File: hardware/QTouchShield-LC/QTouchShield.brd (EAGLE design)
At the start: 101.6 x 81.3 mm, 56 parts, among them IC1 AT32UC3C0512CJEDEC-MS-026, J1 SNS00...07, J10 CAPS08...15, J11 CAPS24...31, J12 CAPS16...23, J13 SPI-MEGA, J14 SPI-UNO, J15 COMMS Select, J16 DETECT00...15, J17 DETECT16...31, J18 JTAG, J19 TOUCH DATA, J2 SNS08...15, J3 SNS16...23, J4 SNS24...31, J5 RES00...07, J6 RES08...15, J7 RES16...23, J8 RES24...31, J9 CAPS00...07, Q1 BSS138, Q2 BSS138, Q3 BSS138, Q4 BSS138, Q5 BSS138, Q6 BSS138, U1 ARDUINO-2560-MEGA-R3-SMD, X1 Firmware Upgrade Port

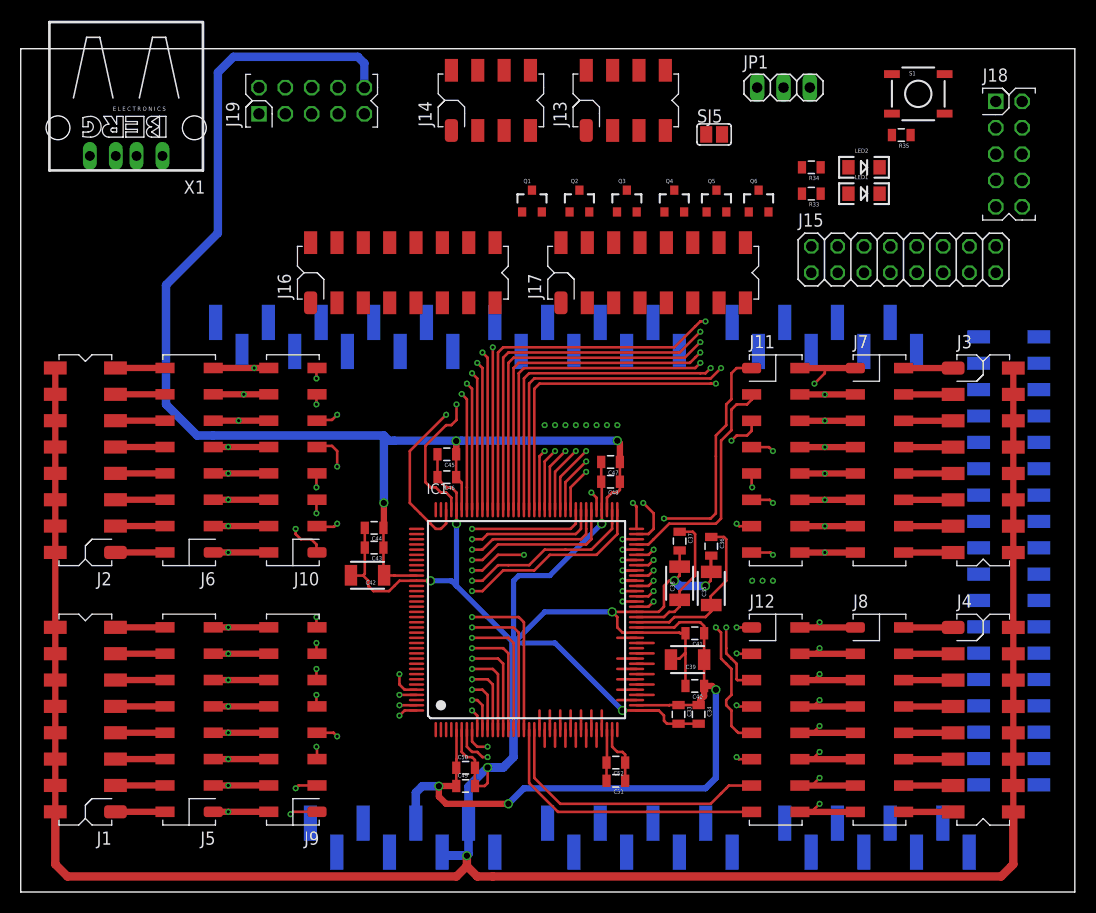
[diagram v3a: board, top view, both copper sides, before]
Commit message: 95% complete routing of board; extra VCC decoupling; USB changes.
Routing about 95% complete.
Added extra 10uF cap in the VCC supply.
Added in-line resistors in the D+/D- lines.
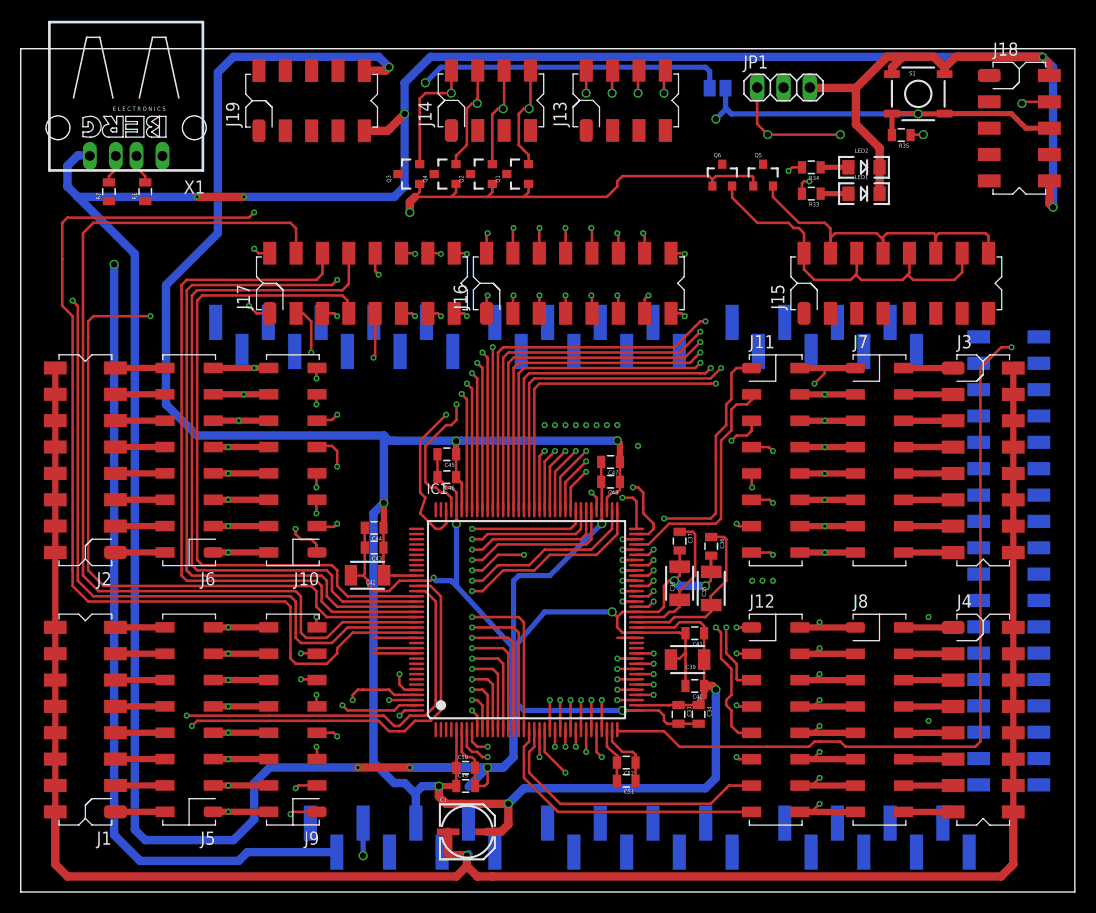
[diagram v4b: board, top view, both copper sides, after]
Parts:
- added C1: 10uF/35V, SparkFun:PANASONIC_C
- added R1, R2: 39R, SparkFun:0805
- J15: device pinhead:2X08 -> codinghead:2X8-V-MALE-SMT-HARWIN
- J18, J19: device codinghead:2X5-V-MALE-THRUHOLE -> codinghead:2X5-V-MALE-SMT-HARWIN
- moved J17 28.1 mm to (24.0, 57.4)
- moved Q4 22.2 mm to (41.0, 69.2), turned to 90 degrees
- moved Q3 21.1 mm to (37.5, 69.2), turned to 90 degrees
- moved J16 17.0 mm to (44.9, 57.4)
- moved J15 10.2 mm to (75.5, 57.4), turned to 90 degrees
- moved Q2 9.76 mm to (44.5, 69.2), turned to 90 degrees
- moved Q5 5.15 mm to (71.6, 69.0)
- moved SJ5 4.47 mm to (67.2, 77.5), flipped to the bottom, turned to 180 degrees
- moved Q6 4.30 mm to (67.6, 69.0)
- moved Q1 2.96 mm to (48.0, 69.2), turned to 90 degrees
- moved J18 2.69 mm to (95.0, 78.7)
- moved C51 1.00 mm to (58.4, 10.7)
- moved C52 1.00 mm to (58.4, 12.5)
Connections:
- new net USB-DM: IC1.50, R1.1
- new net USB-DP: IC1.51, R2.1
- net GND: now also C1.-; no longer U1.GND_2, U1.GND_3, U1.GND_4, U1.GND_5
- net N$34: now also R1.2, X1.2; no longer IC1.51, X1.3
- net N$35: now also R2.2, X1.3; no longer IC1.50, X1.2
- net SHIELD-DETECT16: now also J17.15; no longer J17.1
- net SHIELD-DETECT17: now also J17.16; no longer J17.2
- net SHIELD-DETECT18: now also J17.13; no longer J17.3
- net SHIELD-DETECT19: now also J17.14; no longer J17.4
- net SHIELD-DETECT20: now also J17.11; no longer J17.5
- net SHIELD-DETECT21: now also J17.12; no longer J17.6
- net SHIELD-DETECT22: now also J17.9; no longer J17.7
- net SHIELD-DETECT23: now also J17.10; no longer J17.8
- net SHIELD-DETECT24: now also J17.7; no longer J17.9
- net SHIELD-DETECT25: now also J17.8; no longer J17.10
- net SHIELD-DETECT26: now also J17.5; no longer J17.11
- net SHIELD-DETECT27: now also J17.6; no longer J17.12
- net SHIELD-DETECT28: now also J17.3; no longer J17.13
- net SHIELD-DETECT29: now also J17.4; no longer J17.14
- net SHIELD-DETECT30: now also J17.1; no longer J17.15
- net SHIELD-DETECT31: now also J17.2; no longer J17.16
- net VCC: now also C1.+; no longer U1.5V_2, U1.5V_3
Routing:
- net JTAG_RESET: track 0.00 -> 400.2 mm, vias 0 -> 5
- net GND: track 359.4 -> 649.7 mm, vias 9 -> 16
- net IOREF: track 0.00 -> 151.4 mm, vias 0 -> 2
- net SHIELD-DETECT1: track 1.65 -> 152.7 mm, vias 0 -> 2
- net SHIELD-DETECT3: track 1.65 -> 147.6 mm, vias 0 -> 2
- net SHIELD-DETECT0: track 1.85 -> 140.9 mm, vias 0 -> 2
- net SHIELD-DETECT5: track 1.65 -> 139.9 mm, vias 0 -> 2
- net SHIELD-DETECT2: track 1.85 -> 135.0 mm, vias 0 -> 2
- net SHIELD-DETECT7: track 1.65 -> 133.6 mm, vias 0 -> 2
- net SHIELD-DETECT4: track 1.85 -> 129.0 mm, vias 0 -> 2
- net SHIELD-DATA-TRANSFER-VISUAL-OUTPUT: track 1.65 -> 127.7 mm, vias 0 -> 2
- net SHIELD-DETECT9: track 1.65 -> 127.3 mm, vias 0 -> 2
- net QT-DETECT-GENERAL: track 1.85 -> 126.0 mm, vias 0 -> 2
- net SHIELD-DETECT11: track 0.00 -> 123.6 mm, vias 0 -> 2
- net SHIELD-DETECT21: track 1.65 -> 123.3 mm, vias 0 -> 2
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
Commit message: Split Arduino reset electrically from UC3 & JTAG reset signals.
Split resets. If user wants to reset Arduino from switch, they have to
solder blob the jumper by hand.
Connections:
- new net ARDUINO_RESET: SJ5.1, U1.RESET
- net JTAG_RESET: no longer SJ5.1, U1.RESET
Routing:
- net JTAG_RESET: track 400.2 -> 225.8 mm, vias 5 -> 3
- net ARDUINO_RESET: track 0.00 -> 174.4 mm, vias 0 -> 2
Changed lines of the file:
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@@
 <contactref element="R35" pad="2"/>
 <contactref element="SJ5" pad="2"/>
-<contactref element="SJ5" pad="1"/>
-<contactref element="U1" pad="RESET"/>
 <contactref element="J18" pad="6"/>
 <wire x1="67.932" y1="77.48" x2="67.932" y2="75.568" width="0.5" layer="16"/>
@@
 <wire x1="95.475" y1="75.025" x2="96" y2="74.5" width="0.5" layer="1"/>
 <wire x1="68.5" y1="75" x2="68" y2="75.5" width="0.5" layer="16"/>
-<wire x1="66.408" y1="77.48" x2="66.408" y2="79.092" width="0.5" layer="16"/>
-<wire x1="66.408" y1="79.092" x2="66" y2="79.5" width="0.5" layer="16"/>
-<wire x1="66" y1="79.5" x2="40.5" y2="79.5" width="0.5" layer="16"/>
-<wire x1="40.5" y1="79.5" x2="39" y2="78" width="0.5" layer="16"/>
-<via x="39" y="78" extent="1-16" drill="0.6"/>
-<wire x1="39" y1="78" x2="3.5" y2="78" width="0.5" layer="15"/>
-<wire x1="3.5" y1="78" x2="1.5" y2="76" width="0.5" layer="15"/>
-<wire x1="1.5" y1="76" x2="1.5" y2="5" width="0.5" layer="15"/>
-<wire x1="1.5" y1="5" x2="3" y2="3.5" width="0.5" layer="15"/>
-<wire x1="3" y1="3.5" x2="33" y2="3.5" width="0.5" layer="15"/>
-<via x="33" y="3.5" extent="1-16" drill="0.6"/>
-<wire x1="33" y1="3.5" x2="33" y2="6.64" width="0.5" layer="16"/>
 <wire x1="67.932" y1="77.48" x2="67.932" y2="75.432" width="0.5" layer="16"/>
 <wire x1="67.932" y1="75.432" x2="67.5" y2="75" width="0.5" layer="16"/>
@@
 <wire x1="37.5" y1="18.5" x2="38" y2="18" width="0.5" layer="15"/>
 <wire x1="38" y1="18" x2="38" y2="14" width="0.5" layer="15"/>
-<wire x1="3" y1="3.5" x2="4" y2="4.5" width="0" layer="19" extent="15-15"/>
 </signal>
 <signal name="N$1">
@@
 <wire x1="9.16" y1="69.66" x2="9.16" y2="70.95" width="0.254" layer="1"/>
 </signal>
+<signal name="ARDUINO_RESET">
+<contactref element="SJ5" pad="1"/>
+<contactref element="U1" pad="RESET"/>
+<wire x1="66.408" y1="77.48" x2="66.408" y2="79.092" width="0.5" layer="16"/>
+<wire x1="66.408" y1="79.092" x2="66" y2="79.5" width="0.5" layer="16"/>
+<wire x1="66" y1="79.5" x2="40.5" y2="79.5" width="0.5" layer="16"/>
+<wire x1="40.5" y1="79.5" x2="39" y2="78" width="0.5" layer="16"/>
+<via x="39" y="78" extent="1-16" drill="0.6"/>
+<wire x1="39" y1="78" x2="3.5" y2="78" width="0.5" layer="15"/>
+<wire x1="3.5" y1="78" x2="1.5" y2="76" width="0.5" layer="15"/>
+<wire x1="1.5" y1="76" x2="1.5" y2="5" width="0.5" layer="15"/>
+<wire x1="1.5" y1="5" x2="3" y2="3.5" width="0.5" layer="15"/>
+<wire x1="3" y1="3.5" x2="33" y2="3.5" width="0.5" layer="15"/>
+<via x="33" y="3.5" extent="1-16" drill="0.6"/>
+<wire x1="33" y1="3.5" x2="33" y2="6.64" width="0.5" layer="16"/>
+</signal>
 </signals>

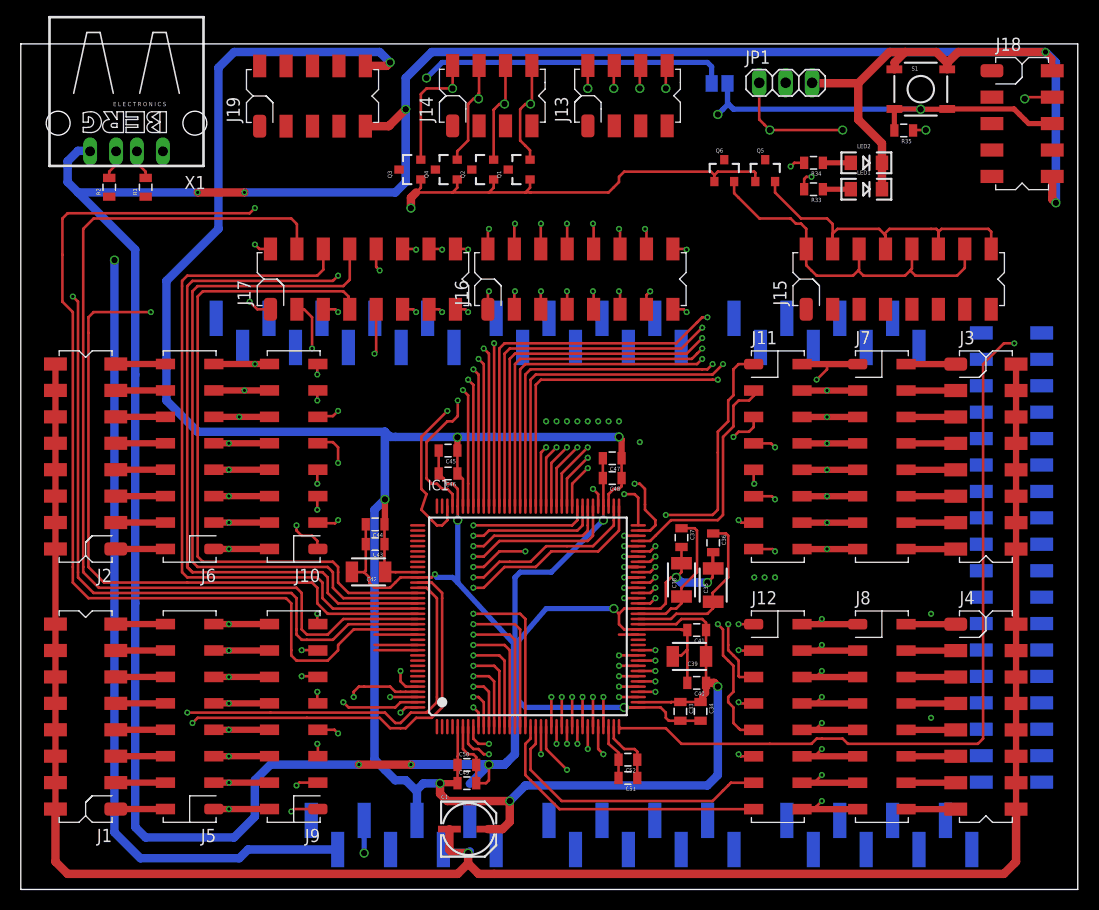
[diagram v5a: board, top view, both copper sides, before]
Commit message: Final routed board for LC version.
Board finally routed with the LC layout.
No known major issues to resolve.
Consider only ground-plane under MCU and review from STROHAL.
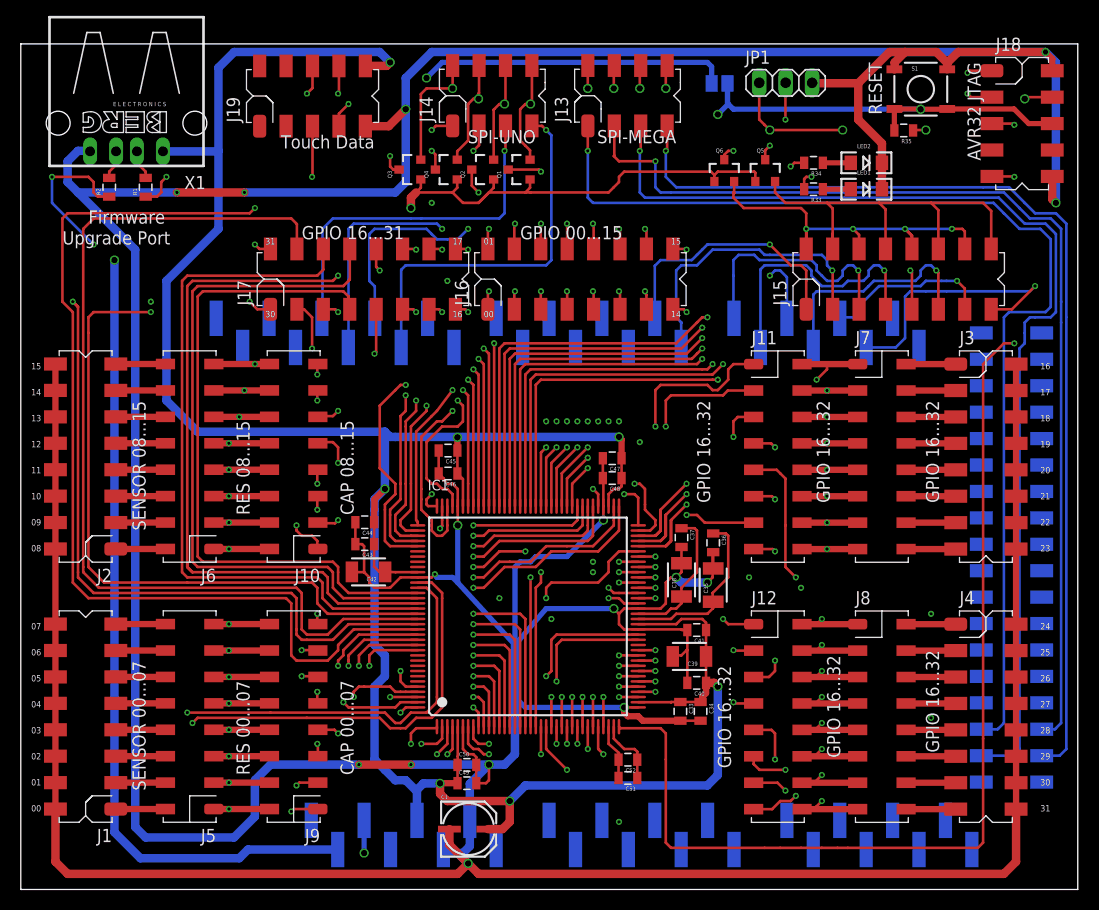
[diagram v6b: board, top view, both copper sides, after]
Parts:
- J1: value SNS00...07 -> SENSOR 00...07
- J10: value CAPS08...15 -> CAP 08...15
- J11: value CAPS24...31 -> CAP 16...23
- J12: value CAPS16...23 -> CAP 24...31
- J2: value SNS08...15 -> SENSOR 08...15
- J3: value SNS16...23 -> SENSOR 16...23
- J4: value SNS24...31 -> SENSOR 24...31
- J5: value RES00...07 -> RES 00...07
- J6: value RES08...15 -> RES 08...15
- J7: value RES16...23 -> RES 16...23
- J8: value RES24...31 -> RES 24...31
- J9: value CAPS00...07 -> CAP 00...07
- moved C44 1.02 mm to (33.1, 35.3)
- moved C43 1.00 mm to (33.1, 33.2)
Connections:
- net GND: now also U1.GND_2
- net SNS16: now also J11.1; no longer J12.15
- net SNS17: now also J11.3; no longer J12.13
- net SNS18: now also J11.5; no longer J12.11
- net SNS19: now also J11.7; no longer J12.9
- net SNS20: now also J11.9; no longer J12.7
- net SNS21: now also J11.11; no longer J12.5
- net SNS22: now also J11.13; no longer J12.3
- net SNS23: now also J11.15; no longer J12.1
- net SNS24: now also J12.1; no longer J11.15
- net SNS25: now also J12.3; no longer J11.13
- net SNS26: now also J12.5; no longer J11.11
- net SNS27: now also J12.7; no longer J11.9
- net SNS28: now also J12.9; no longer J11.7
- net SNS29: now also J12.11; no longer J11.5
- net SNS30: now also J12.13; no longer J11.3
- net SNS31: now also J12.15; no longer J11.1
- net VCC: now also X1.1
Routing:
- net JTAG_TCK: track 0.00 -> 146.5 mm, vias 0 -> 2
- net USB-DM: track 0.00 -> 142.8 mm, vias 0 -> 2
- net JTAG_TDO: track 0.00 -> 138.4 mm, vias 0 -> 2
- net USB-DP: track 1.85 -> 139.7 mm, vias 0 -> 3
- net JTAG_TDI: track 0.00 -> 130.5 mm, vias 0 -> 2
- net JTAG_TMS: track 0.00 -> 129.4 mm, vias 0 -> 2
- net TOUCH_DATA-SCK: track 0.00 -> 126.4 mm, vias 0 -> 2
- net TOUCH_DATA-MISO: track 4.15 -> 129.7 mm, vias 0 -> 2
- net TOUCH_DATA-MOSI: track 4.15 -> 125.1 mm, vias 0 -> 2
- net TOUCH_DATA-SS: track 4.15 -> 116.9 mm, vias 0 -> 2
- net MISO-MEGA: track 0.00 -> 105.9 mm, vias 0 -> 1
- net SCK-MEGA: track 0.00 -> 104.2 mm, vias 0 -> 1
- net MOSI-MEGA: track 0.00 -> 99.9 mm, vias 0 -> 1
- net SS-MEGA: track 0.00 -> 98.5 mm, vias 0 -> 1
- net SDT-USART0-TXD: track 0.00 -> 74.9 mm, vias 0 -> 2
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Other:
- board text added: "00"
- board text added: "01"
- board text added: "02"
- board text added: "03"
- board text added: "04"
- board text added: "05"
- board text added: "06"
- board text added: "07"
- board text added: "08"
- board text added: "09"
- board text added: "10"
- board text added: "11"
- board text added: "12"
- board text added: "13"
- board text added: "14"
- board text added: "15"
- board text added: "16"
- board text added: "17"
- board text added: "18"
- board text added: "19"
- board text added: "20"
- board text added: "21"
- board text added: "22"
- board text added: "23"
- board text added: "24"
- board text added: "25"
- board text added: "26"
- board text added: "27"
- board text added: "28"
- board text added: "29"
- board text added: "30"
- board text added: "31"
- board text added: "AVR32 JTAG"
- board text added: "CAP 00...07"
- board text added: "CAP 08...15"
- board text added: "Firmware"
- board text added: "GPIO 00...15"
- board text added: "GPIO 16...31"
- board text added: "GPIO 16...32"
- board text added: "RES 00...07"
- board text added: "RES 08...15"
- board text added: "RESET"
- board text added: "SENSOR 00...07"
- board text added: "SENSOR 08...15"
- board text added: "SPI-MEGA"
- board text added: "SPI-UNO"
- board text added: "Touch Data"
- board text added: "Upgrade Port"
